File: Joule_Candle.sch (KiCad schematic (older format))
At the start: 6 parts, among them Q1 BC817-40

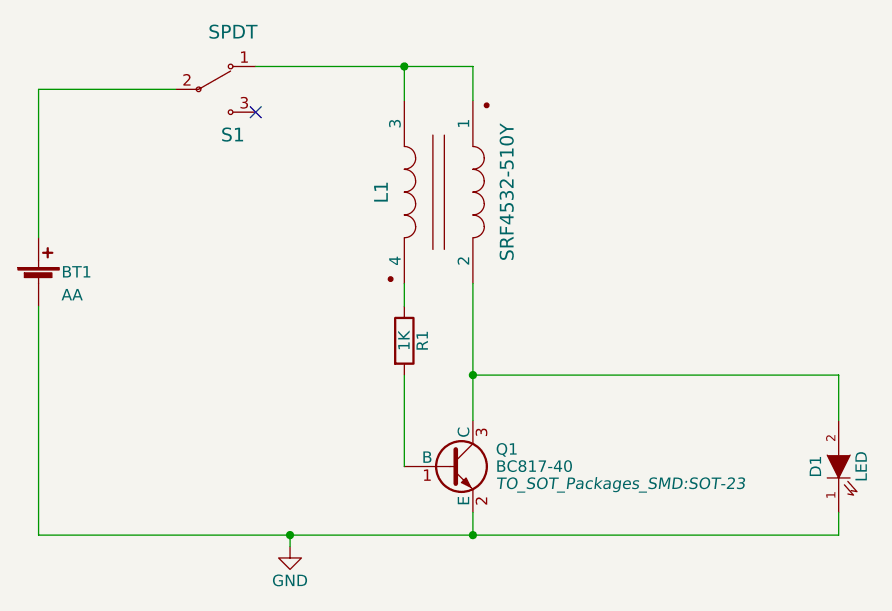
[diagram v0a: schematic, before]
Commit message: change value of R1
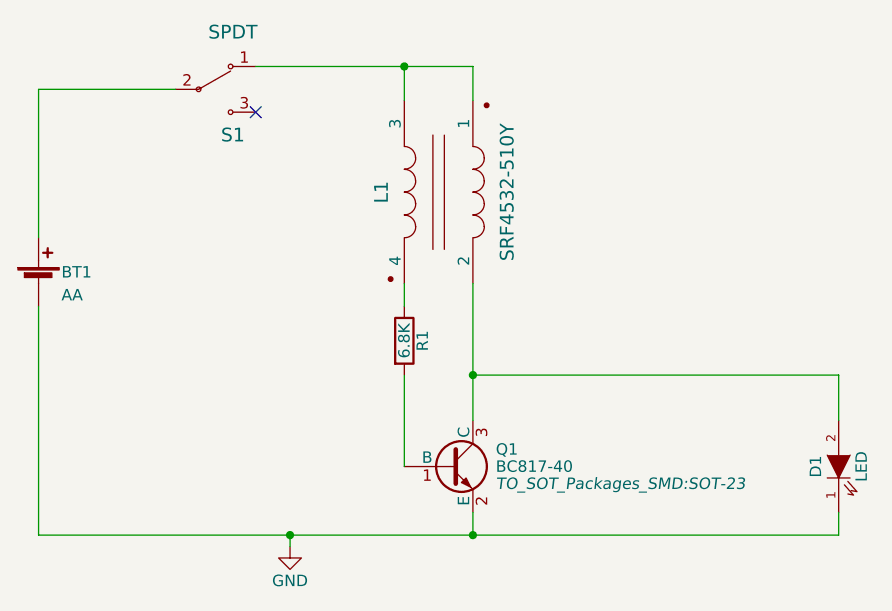
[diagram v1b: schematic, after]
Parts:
- R1: value 1K -> 6.8K
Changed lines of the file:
@@
 P 5900 4200
 F 0 "R1" V 5980 4200 50  0000 C CNN
-F 1 "1K" V 5900 4200 50  0000 C CNN
+F 1 "6.8K" V 5900 4200 50  0000 C CNN
 F 2 "Resistors_SMD:R_0603_HandSoldering" V 5830 4200 50  0001 C CNN
 F 3 "" H 5900 4200 50  0000 C CNN

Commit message: update schematic with part info. Add datasheets to dir
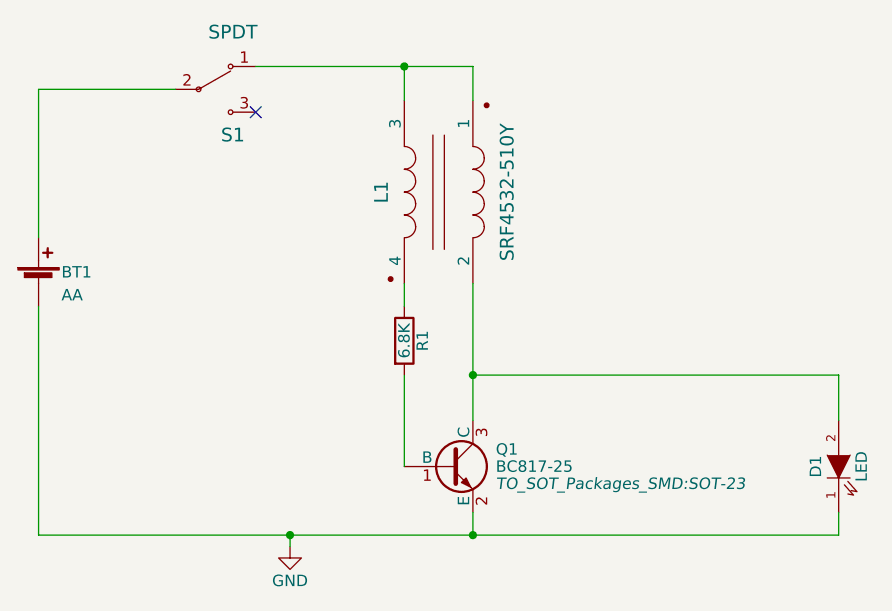
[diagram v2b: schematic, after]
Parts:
- BT1: Description NONE -> BATTERY CONTACT AA SIZE; Manufacture NONE -> Memory Protected Devices; Mfg Part Number NONE -> BK-92; Package NONE -> THT
- D1: Description (none) -> Warm White 3mm; Manufacture (none) -> NONE; Mfg Part Number (none) -> NONE; Package (none) -> 3mm THT
- L1: Description (none) -> CMC 51UH 200MA 2LN 2 KOHM SMD; Manufacture (none) -> Bourns; Mfg Part Number (none) -> SRF4532-510Y; Package (none) -> SMD
- Q1: value BC817-40 -> BC817-25; Description (none) -> TRANS NPN 45V 0.8A SOT-23; Manufacture (none) -> Micro Commercial; Mfg Part Number (none) -> BC817-25-TP; Package (none) -> SOT-23
- R1: Description NONE -> RES SMD 6.8K OHM 5% 1/10W 0603; Manufacture NONE -> Yageo; Mfg Part Number NONE -> RC0603JR-076K8L; Package NONE -> 0603
- S1: Description (none) -> SWITCH SLIDE SPDT 100MA 12V; Manufacture (none) -> C&K; Mfg Part Number (none) -> OS102011MA1QN1; Package (none) -> PC PIN
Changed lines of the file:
@@
 F 2 "Battery:AA_PCB-Clip" V 4300 3990 50  0001 C CNN
 F 3 "" V 4300 3990 50  0000 C CNN
-F 4 "NONE" H 4300 3950 60  0001 C CNN "Manufacture"
-F 5 "NONE" H 4300 3950 60  0001 C CNN "Mfg Part Number"
-F 6 "NONE" H 4300 3950 60  0001 C CNN "Package"
-F 7 "NONE" H 4300 3950 60  0001 C CNN "Description"
+F 4 "Memory Protected Devices" H 4300 3950 60  0001 C CNN "Manufacture"
+F 5 "BK-92" H 4300 3950 60  0001 C CNN "Mfg Part Number"
+F 6 "THT" H 4300 3950 60  0001 C CNN "Package"
+F 7 "BATTERY CONTACT AA SIZE" H 4300 3950 60  0001 C CNN "Description"
 	1    4300 3950
 	1    0    0    -1
@@
 F 2 "Resistors_SMD:R_0603_HandSoldering" V 5830 4200 50  0001 C CNN
 F 3 "" H 5900 4200 50  0000 C CNN
-F 4 "NONE" H 5900 4200 60  0001 C CNN "Manufacture"
-F 5 "NONE" H 5900 4200 60  0001 C CNN "Mfg Part Number"
-F 6 "NONE" H 5900 4200 60  0001 C CNN "Package"
-F 7 "NONE" H 5900 4200 60  0001 C CNN "Description"
+F 4 "Yageo" H 5900 4200 60  0001 C CNN "Manufacture"
+F 5 "RC0603JR-076K8L" H 5900 4200 60  0001 C CNN "Mfg Part Number"
+F 6 "0603" H 5900 4200 60  0001 C CNN "Package"
+F 7 "RES SMD 6.8K OHM 5% 1/10W 0603" H 5900 4200 60  0001 C CNN "Description"
 	1    5900 4200
 	1    0    0    -1
@@
 F 2 "LEDs:3mm_PCB_Edge" H 7800 4750 50  0001 C CNN
 F 3 "" H 7800 4750 50  0000 C CNN
+F 4 "NONE" H 7800 4750 60  0001 C CNN "Manufacture"
+F 5 "NONE" H 7800 4750 60  0001 C CNN "Mfg Part Number"
+F 6 "3mm THT" H 7800 4750 60  0001 C CNN "Package"
+F 7 "Warm White 3mm" H 7800 4750 60  0001 C CNN "Description"
 	1    7800 4750
 	0    -1   -1   0
@@
 P 6100 4750
 F 0 "Q1" H 6300 4825 50  0000 L CNN
-F 1 "BC817-40" H 6300 4750 50  0000 L CNN
+F 1 "BC817-25" H 6300 4750 50  0000 L CNN
 F 2 "TO_SOT_Packages_SMD:SOT-23" H 6300 4675 50  0000 L CIN
 F 3 "" H 6100 4750 50  0000 L CNN
+F 4 "Micro Commercial" H 6100 4750 60  0001 C CNN "Manufacture"
+F 5 "BC817-25-TP" H 6100 4750 60  0001 C CNN "Mfg Part Number"
+F 6 "SOT-23" H 6100 4750 60  0001 C CNN "Package"
+F 7 "TRANS NPN 45V 0.8A SOT-23" H 6100 4750 60  0001 C CNN "Description"
 	1    6100 4750
 	1    0    0    -1
@@
 F 2 "Inductor:SRF4532-510Y" H 6050 3550 60  0001 C CNN
 F 3 "" H 6050 3550 60  0000 C CNN
+F 4 "Bourns" H 6050 3550 60  0001 C CNN "Manufacture"
+F 5 "SRF4532-510Y" H 6050 3550 60  0001 C CNN "Mfg Part Number"
+F 6 "SMD" H 6050 3550 60  0001 C CNN "Package"
+F 7 "CMC 51UH 200MA 2LN 2 KOHM SMD" H 6050 3550 60  0001 C CNN "Description"
 	1    6050 3550
 	0    1    1    0
@@
 F 2 "Switches:SPDT_OS102011MA1QN1" H 5150 3100 60  0001 C CNN
 F 3 "" H 5150 3100 60  0000 C CNN
+F 4 "C&K" H 5150 3100 60  0001 C CNN "Manufacture"
+F 5 "OS102011MA1QN1" H 5150 3100 60  0001 C CNN "Mfg Part Number"
+F 6 "PC PIN" H 5150 3100 60  0001 C CNN "Package"
+F 7 "SWITCH SLIDE SPDT 100MA 12V" H 5150 3100 60  0001 C CNN "Description"
 	1    5150 3100
 	1    0    0    -1
